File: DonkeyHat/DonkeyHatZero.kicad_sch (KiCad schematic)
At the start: 12 parts, among them J1 GPIO, J2 Conn_01x02_Pin, J3 Conn_01x02_Pin, J4 Conn_02x03_Top_Bottom, J5 Battery +, J6 Battery -, J7 +5v, J8 GND, U2 rp2040-zero

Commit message: Added latest prod version
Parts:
- J4: footprint Connector_PinHeader_1.00mm:PinHeader_2x03_P1.00mm_Vertical -> Connector_PinHeader_2.54mm:PinHeader_2x03_P2.54mm_Vertical
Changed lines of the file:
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@@
 			)
 		)
-		(property "Footprint" "Connector_PinHeader_1.00mm:PinHeader_2x03_P1.00mm_Vertical"
+		(property "Footprint" "Connector_PinHeader_2.54mm:PinHeader_2x03_P2.54mm_Vertical"
 			(at 162.56 104.14 0)
 			(effects

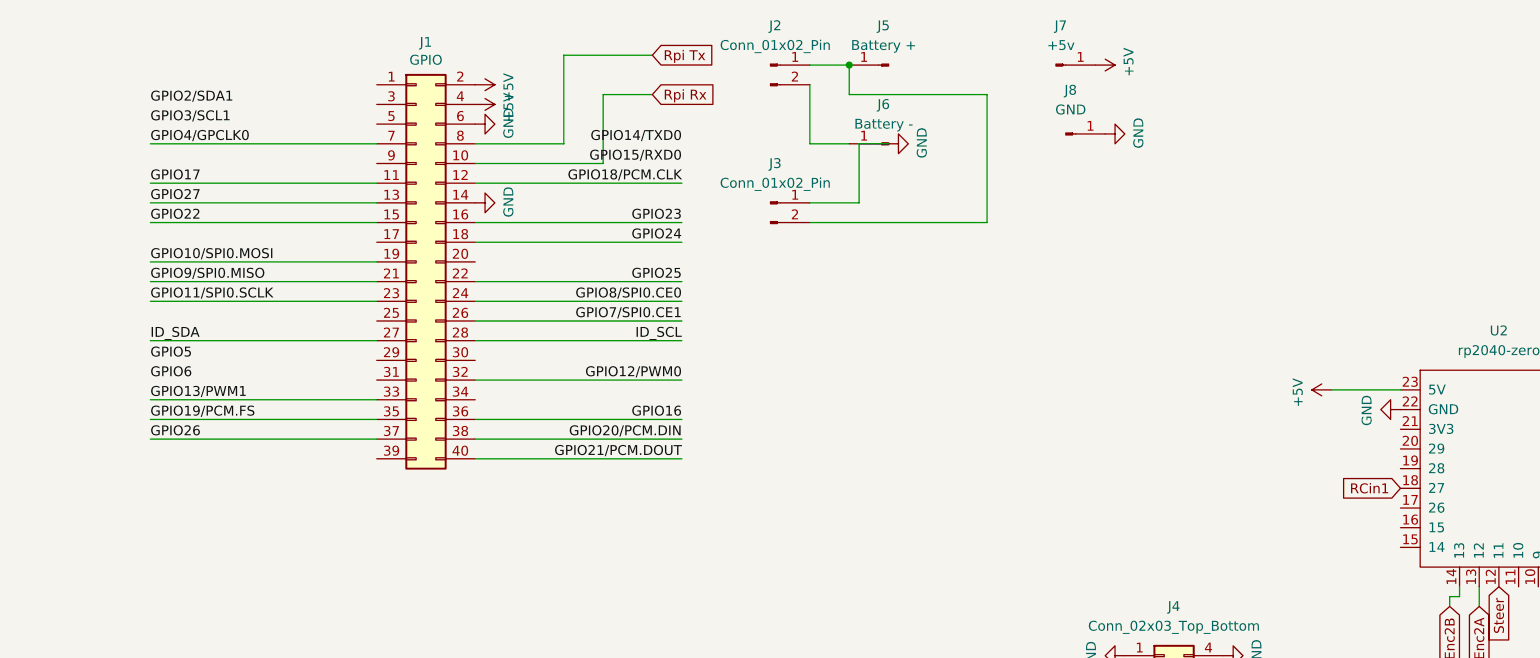
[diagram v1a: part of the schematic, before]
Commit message: Added OLED
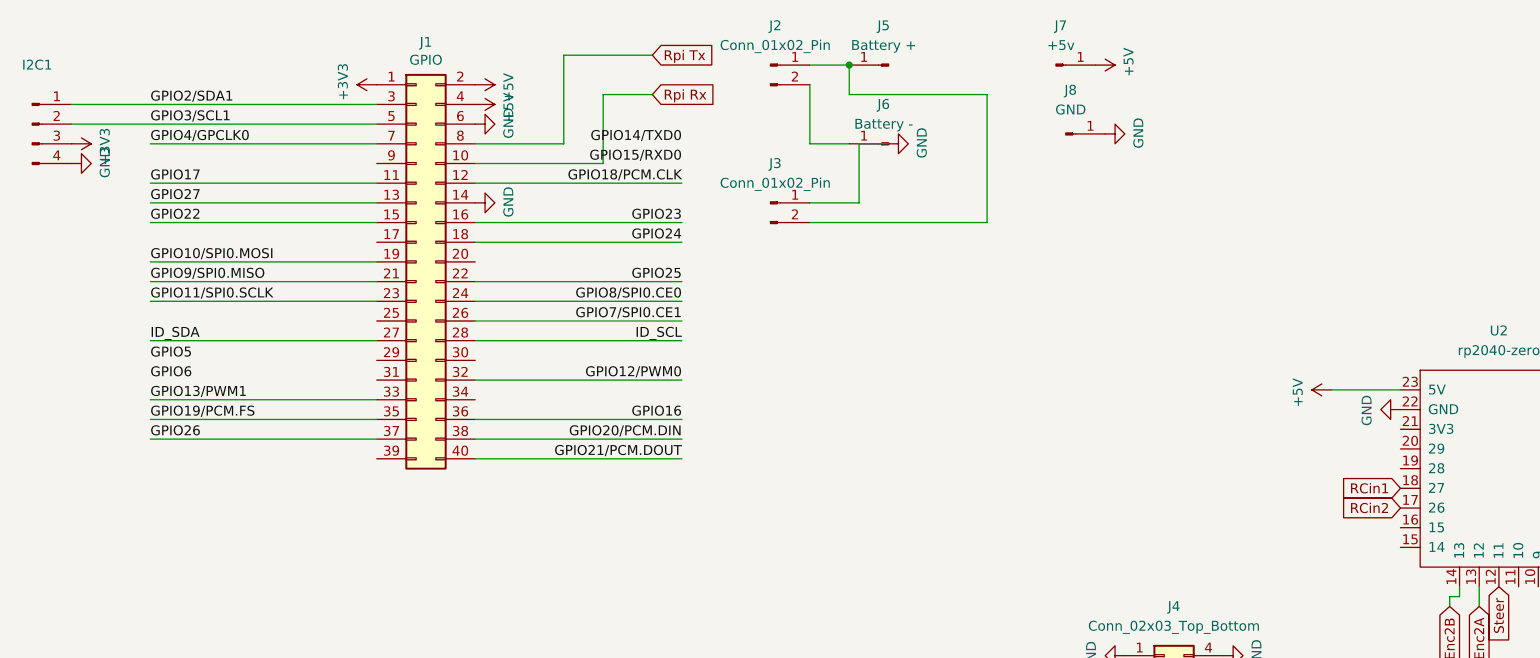
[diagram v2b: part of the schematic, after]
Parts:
- added I2C1: Conn_01x04_Pin, Connector_PinHeader_2.54mm:PinHeader_1x04_P2.54mm_Vertical, symbol Connector:Conn_01x04_Pin
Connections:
- net GND: now also I2C1.4 (Pin_4)
- net GPIO2/SDA1: now also J1.3 (Pin_3), I2C1.1 (Pin_1)
- net GPIO3/SCL1: now also J1.5 (Pin_5), I2C1.2 (Pin_2)
- net +3V3: now reaches J1.1 (Pin_1)
- net +3V3: now also I2C1.3 (Pin_3)
- net RCin2: now reaches U2.17 (26)
